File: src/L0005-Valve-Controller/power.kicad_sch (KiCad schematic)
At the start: 29 parts, among them P16 647676-2, P2 140-504-415-000, P9 647676-2, U2 LMS8117AMP-3.3_NOPB, U5 Optocoupler

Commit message: plotted schematic to pdf
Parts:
- C10: value (none) -> 0.1uF
- C11, C14: value (none) -> 2.2uF
- C12, C13: value (none) -> 2.2uF; footprint (none) -> L0005-Valve-Controller:CAP_0603
- C3, C6, C7: value (none) -> 0.1uF; footprint (none) -> L0005-Valve-Controller:CAP_0603
- C8: value (none) -> 4.7uF
- C9: value (none) -> 1uF
- U2: value LMS8117AMP-3.3_NOPB -> (none); footprint L0005-Valve-Controller:LMS8117AMP-3.3NOPB -> (none)
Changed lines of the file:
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@@
       (effects (font (size 1.27 1.27)) (justify left))
     )
-    (property "Value" "" (id 1) (at 154.305 66.04 90)
+    (property "Value" "0.1uF" (id 1) (at 154.305 66.04 90)
       (effects (font (size 1.27 1.27)) (justify left))
     )
@@
       (effects (font (size 1.27 1.27)) (justify left))
     )
-    (property "Value" "" (id 1) (at 166.37 66.04 90)
-      (effects (font (size 1.27 1.27)) (justify left))
-    )
-    (property "Footprint" "" (id 2) (at 163.83 62.23 0)
+    (property "Value" "0.1uF" (id 1) (at 166.37 66.04 90)
+      (effects (font (size 1.27 1.27)) (justify left))
+    )
+    (property "Footprint" "L0005-Valve-Controller:CAP_0603" (id 2) (at 163.83 62.23 0)
       (effects (font (size 1.27 1.27)) (justify left bottom) hide)
     )
@@
       (effects (font (size 1.27 1.27)) (justify left))
     )
-    (property "Value" "" (id 1) (at 245.745 59.69 90)
+    (property "Value" "2.2uF" (id 1) (at 245.745 59.69 90)
       (effects (font (size 1.27 1.27)) (justify left))
     )
@@
       (effects (font (size 1.27 1.27)) (justify left))
     )
-    (property "Value" "" (id 1) (at 203.835 59.69 90)
+    (property "Value" "2.2uF" (id 1) (at 203.835 59.69 90)
       (effects (font (size 1.27 1.27)) (justify left))
     )
@@
       (effects (font (size 1.27 1.27)) (justify left))
     )
-    (property "Value" "" (id 1) (at 215.9 59.69 90)
-      (effects (font (size 1.27 1.27)) (justify left))
-    )
-    (property "Footprint" "" (id 2) (at 213.36 55.88 0)
+    (property "Value" "2.2uF" (id 1) (at 215.9 59.69 90)
+      (effects (font (size 1.27 1.27)) (justify left))
+    )
+    (property "Footprint" "L0005-Valve-Controller:CAP_0603" (id 2) (at 213.36 55.88 0)
       (effects (font (size 1.27 1.27)) (justify left bottom) hide)
     )
@@
       (effects (font (size 1.27 1.27)) (justify left))
     )
-    (property "Value" "" (id 1) (at 234.315 59.69 90)
-      (effects (font (size 1.27 1.27)) (justify left))
-    )
-    (property "Footprint" "" (id 2) (at 231.775 55.88 0)
+    (property "Value" "2.2uF" (id 1) (at 234.315 59.69 90)
+      (effects (font (size 1.27 1.27)) (justify left))
+    )
+    (property "Footprint" "L0005-Valve-Controller:CAP_0603" (id 2) (at 231.775 55.88 0)
       (effects (font (size 1.27 1.27)) (justify left bottom) hide)
     )
@@
       (effects (font (size 1.27 1.27)) (justify left))
     )
-    (property "Value" "" (id 1) (at 127 66.04 90)
+    (property "Value" "4.7uF" (id 1) (at 127 66.04 90)
       (effects (font (size 1.27 1.27)) (justify left))
     )
@@
       (effects (font (size 1.27 1.27)) (justify left))
     )
-    (property "Value" "" (id 1) (at 127.635 51.435 90)
-      (effects (font (size 1.27 1.27)) (justify left))
-    )
-    (property "Footprint" "" (id 2) (at 125.095 47.625 0)
+    (property "Value" "0.1uF" (id 1) (at 127.635 51.435 90)
+      (effects (font (size 1.27 1.27)) (justify left))
+    )
+    (property "Footprint" "L0005-Valve-Controller:CAP_0603" (id 2) (at 125.095 47.625 0)
       (effects (font (size 1.27 1.27)) (justify left bottom) hide)
     )
@@
       (effects (font (size 1.27 1.27)) (justify left))
     )
-    (property "Value" "" (id 1) (at 140.97 66.04 90)
+    (property "Value" "1uF" (id 1) (at 140.97 66.04 90)
       (effects (font (size 1.27 1.27)) (justify left))
     )
@@
       (effects (font (size 1.27 1.27)) (justify left))
     )
-    (property "Value" "" (id 1) (at 165.735 51.435 90)
-      (effects (font (size 1.27 1.27)) (justify left))
-    )
-    (property "Footprint" "" (id 2) (at 163.195 47.625 0)
+    (property "Value" "0.1uF" (id 1) (at 165.735 51.435 90)
+      (effects (font (size 1.27 1.27)) (justify left))
+    )
+    (property "Footprint" "L0005-Valve-Controller:CAP_0603" (id 2) (at 163.195 47.625 0)
       (effects (font (size 1.27 1.27)) (justify left bottom) hide)
     )
@@
     (in_bom yes) (on_board yes)
     (property "Reference" "U2" (id 0) (at 55.88 48.3108 0))
-    (property "Value" "LMS8117AMP-3.3_NOPB" (id 1) (at 55.88 48.2854 0)
-      (effects (font (size 1.27 1.27)) hide)
-    )
-    (property "Footprint" "L0005-Valve-Controller:LMS8117AMP-3.3NOPB" (id 2) (at 55.88 53.975 0)
-      (effects (font (size 1.27 1.27)) hide)
-    )
+    (property "Value" "" (id 1) (at 55.88 48.2854 0)
+      (effects (font (size 1.27 1.27)) hide)
+    )
+    (property "Footprint" "" (id 2) (at 55.88 53.975 0)
+      (effects (font (size 1.27 1.27)) hide)
+    )

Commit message: routed rev 2
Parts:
- C10, C11, C14, C8, C9: footprint (none) -> L0005-Valve-Controller:CAP_0603
- U2: value (none) -> LMS8117AMP-3.3_NOPB; footprint (none) -> L0005-Valve-Controller:LMS8117AMP-3.3NOPB
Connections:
- net Earth: now also C11.1, C12.1, C13.1, C14.1
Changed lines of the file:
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@@
   (junction (at 223.52 63.5) (diameter 0) (color 0 0 0 0)
   )
+  (junction (at 232.41 63.5) (diameter 0) (color 0 0 0 0)
+  )
   (junction (at 151.13 45.085) (diameter 0) (color 0 0 0 0)
   )
@@
     (stroke (width 0) (type default) (color 0 0 0 0))
   )
-  (wire (pts (xy 223.52 63.5) (xy 241.935 63.5))
+  (wire (pts (xy 223.52 63.5) (xy 232.41 63.5))
     (stroke (width 0) (type default) (color 0 0 0 0))
   )
@@
     (stroke (width 0) (type default) (color 0 0 0 0))
   )
+  (wire (pts (xy 232.41 63.5) (xy 241.935 63.5))
+    (stroke (width 0) (type default) (color 0 0 0 0))
+  )
   (wire (pts (xy 235.585 53.34) (xy 241.935 53.34))
     (stroke (width 0) (type default) (color 0 0 0 0))
@@
   )
   (polyline (pts (xy 22.225 141.605) (xy 22.225 93.345))
+    (stroke (width 0) (type default) (color 0 0 0 0))
+  )
+  (wire (pts (xy 232.41 63.5) (xy 232.41 65.405))
     (stroke (width 0) (type default) (color 0 0 0 0))
   )
@@
       (effects (font (size 1.27 1.27)) (justify left))
     )
-    (property "Footprint" "" (id 2) (at 151.765 62.23 0)
+    (property "Footprint" "L0005-Valve-Controller:CAP_0603" (id 2) (at 151.765 62.23 0)
       (effects (font (size 1.27 1.27)) (justify left bottom) hide)
     )
@@
       (effects (font (size 1.27 1.27)) (justify left))
     )
-    (property "Footprint" "" (id 2) (at 243.205 55.88 0)
+    (property "Footprint" "L0005-Valve-Controller:CAP_0603" (id 2) (at 243.205 55.88 0)
       (effects (font (size 1.27 1.27)) (justify left bottom) hide)
     )
@@
       (effects (font (size 1.27 1.27)) (justify left))
     )
-    (property "Footprint" "" (id 2) (at 201.295 55.88 0)
+    (property "Footprint" "L0005-Valve-Controller:CAP_0603" (id 2) (at 201.295 55.88 0)
       (effects (font (size 1.27 1.27)) (justify left bottom) hide)
     )
@@
       (effects (font (size 1.27 1.27)) (justify left))
     )
-    (property "Footprint" "" (id 2) (at 125.095 62.23 0)
+    (property "Footprint" "L0005-Valve-Controller:CAP_0603" (id 2) (at 125.095 62.23 0)
       (effects (font (size 1.27 1.27)) (justify left bottom) hide)
     )
@@
       (effects (font (size 1.27 1.27)) (justify left))
     )
-    (property "Footprint" "" (id 2) (at 137.16 62.23 0)
+    (property "Footprint" "L0005-Valve-Controller:CAP_0603" (id 2) (at 137.16 62.23 0)
       (effects (font (size 1.27 1.27)) (justify left bottom) hide)
     )
@@
     (pin "1")
     (pin "2")
+  )
+  (symbol (lib_id "L0005-Valve-Controller:Earth") (at 232.41 65.405 0) (unit 1)
+    (in_bom yes) (on_board yes)
+    (property "Reference" "#PWR?" (id 0) (at 232.41 71.755 0)
+      (effects (font (size 1.27 1.27)) hide)
+    )
+    (property "Value" "Earth" (id 1) (at 232.41 69.215 0)
+      (effects (font (size 1.27 1.27)) hide)
+    )
+    (property "Footprint" "" (id 2) (at 232.41 65.405 0)
+      (effects (font (size 1.27 1.27)) hide)
+    )
+    (property "Datasheet" "" (id 3) (at 232.41 65.405 0)
+      (effects (font (size 1.27 1.27)) hide)
+    )
+    (pin "1")
   )
   (symbol (lib_id "L0005-Valve-Controller:LED_GREEN") (at 86.995 60.325 0) (unit 1)
@@
     (in_bom yes) (on_board yes)
     (property "Reference" "U2" (id 0) (at 55.88 48.3108 0))
-    (property "Value" "" (id 1) (at 55.88 48.2854 0)
-      (effects (font (size 1.27 1.27)) hide)
-    )
-    (property "Footprint" "" (id 2) (at 55.88 53.975 0)
-      (effects (font (size 1.27 1.27)) hide)
-    )
+    (property "Value" "LMS8117AMP-3.3_NOPB" (id 1) (at 55.88 48.2854 0)
+      (effects (font (size 1.27 1.27)) hide)
+    )
+    (property "Footprint" "L0005-Valve-Controller:LMS8117AMP-3.3NOPB" (id 2) (at 55.88 53.975 0)
+      (effects (font (size 1.27 1.27)) hide)
+    )

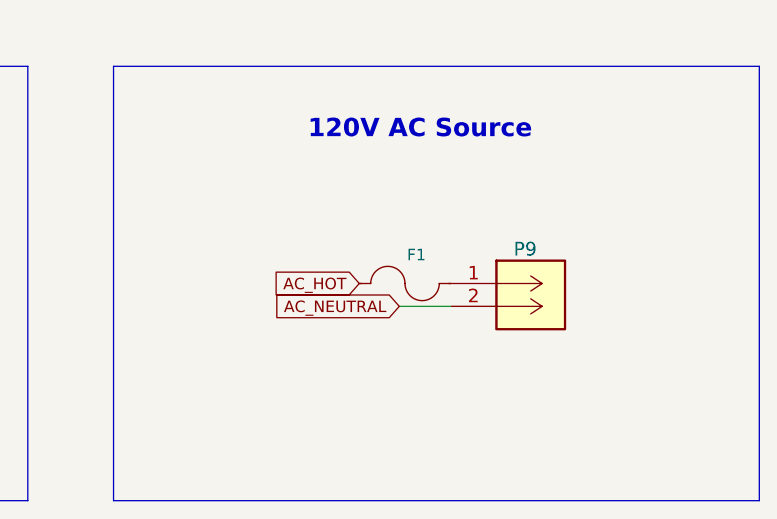
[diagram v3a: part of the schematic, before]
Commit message: added NO jumper to MCU reset button
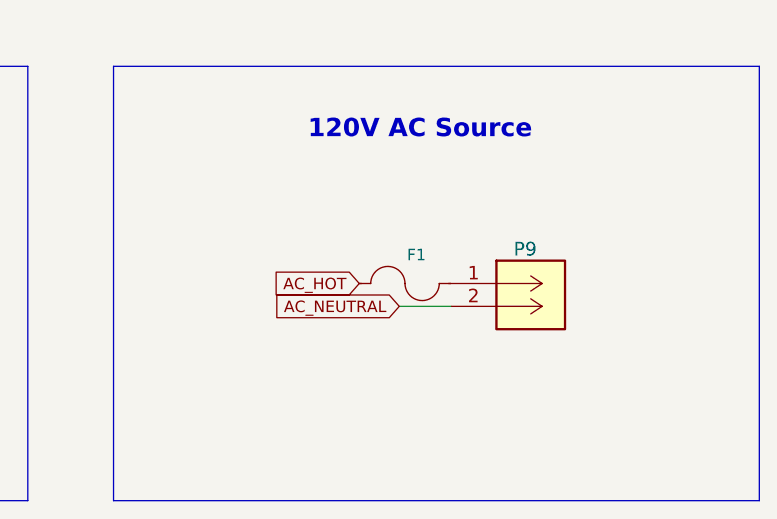
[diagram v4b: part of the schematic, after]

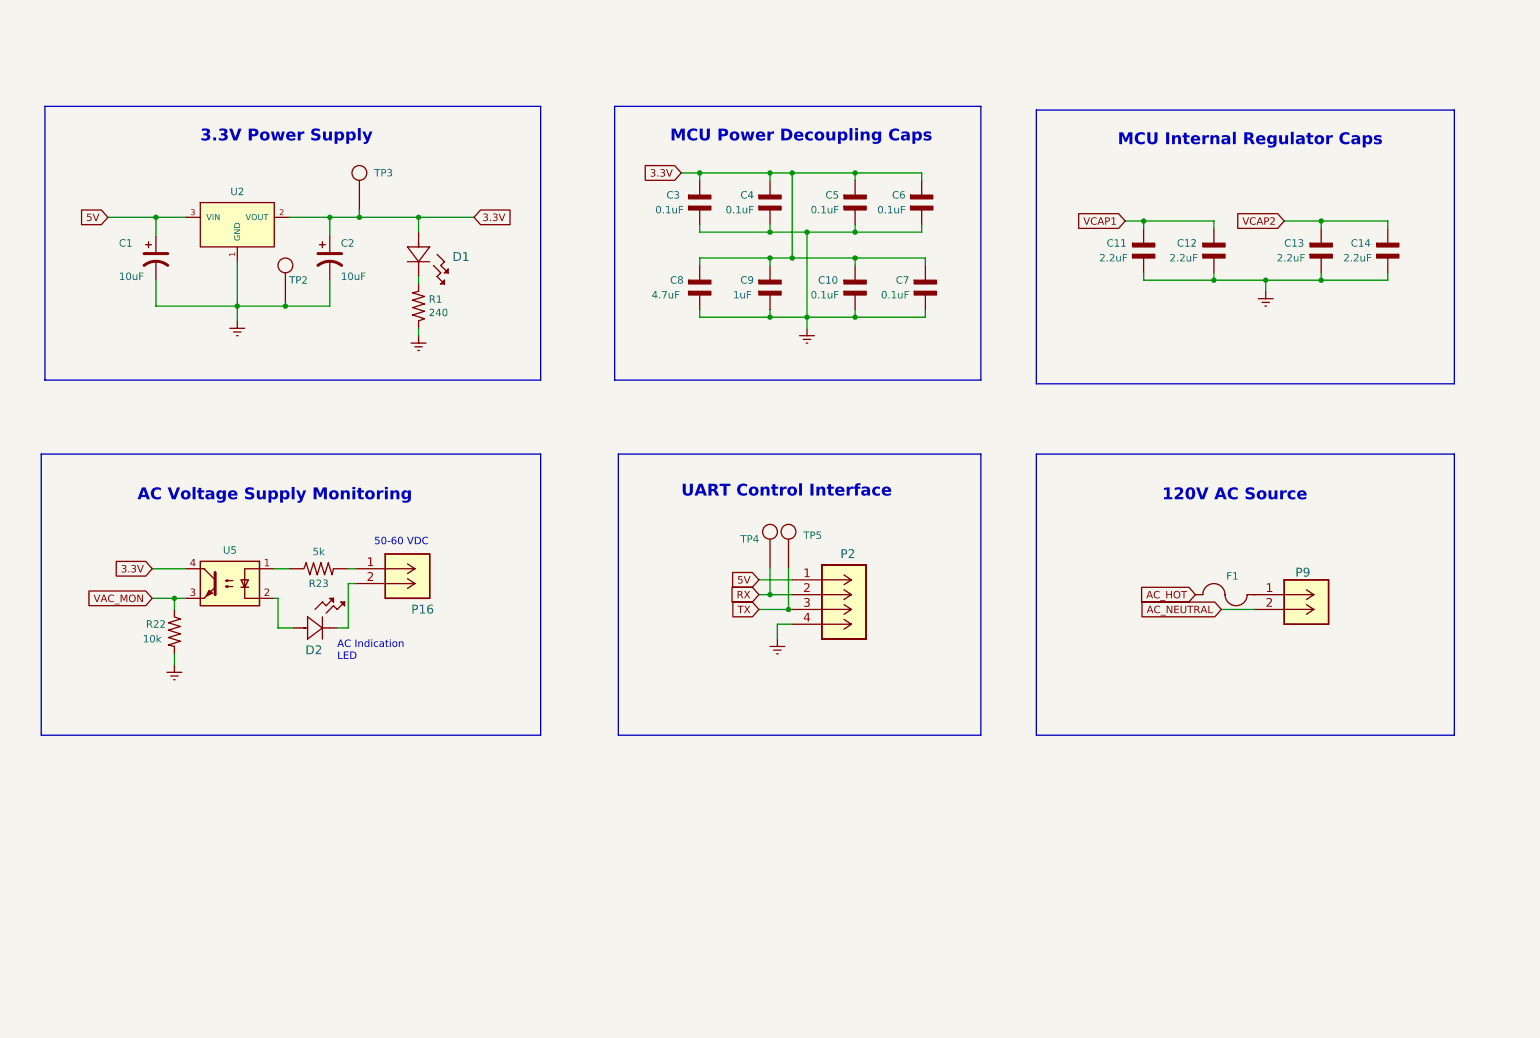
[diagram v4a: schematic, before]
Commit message: added USB to lib files and schematic
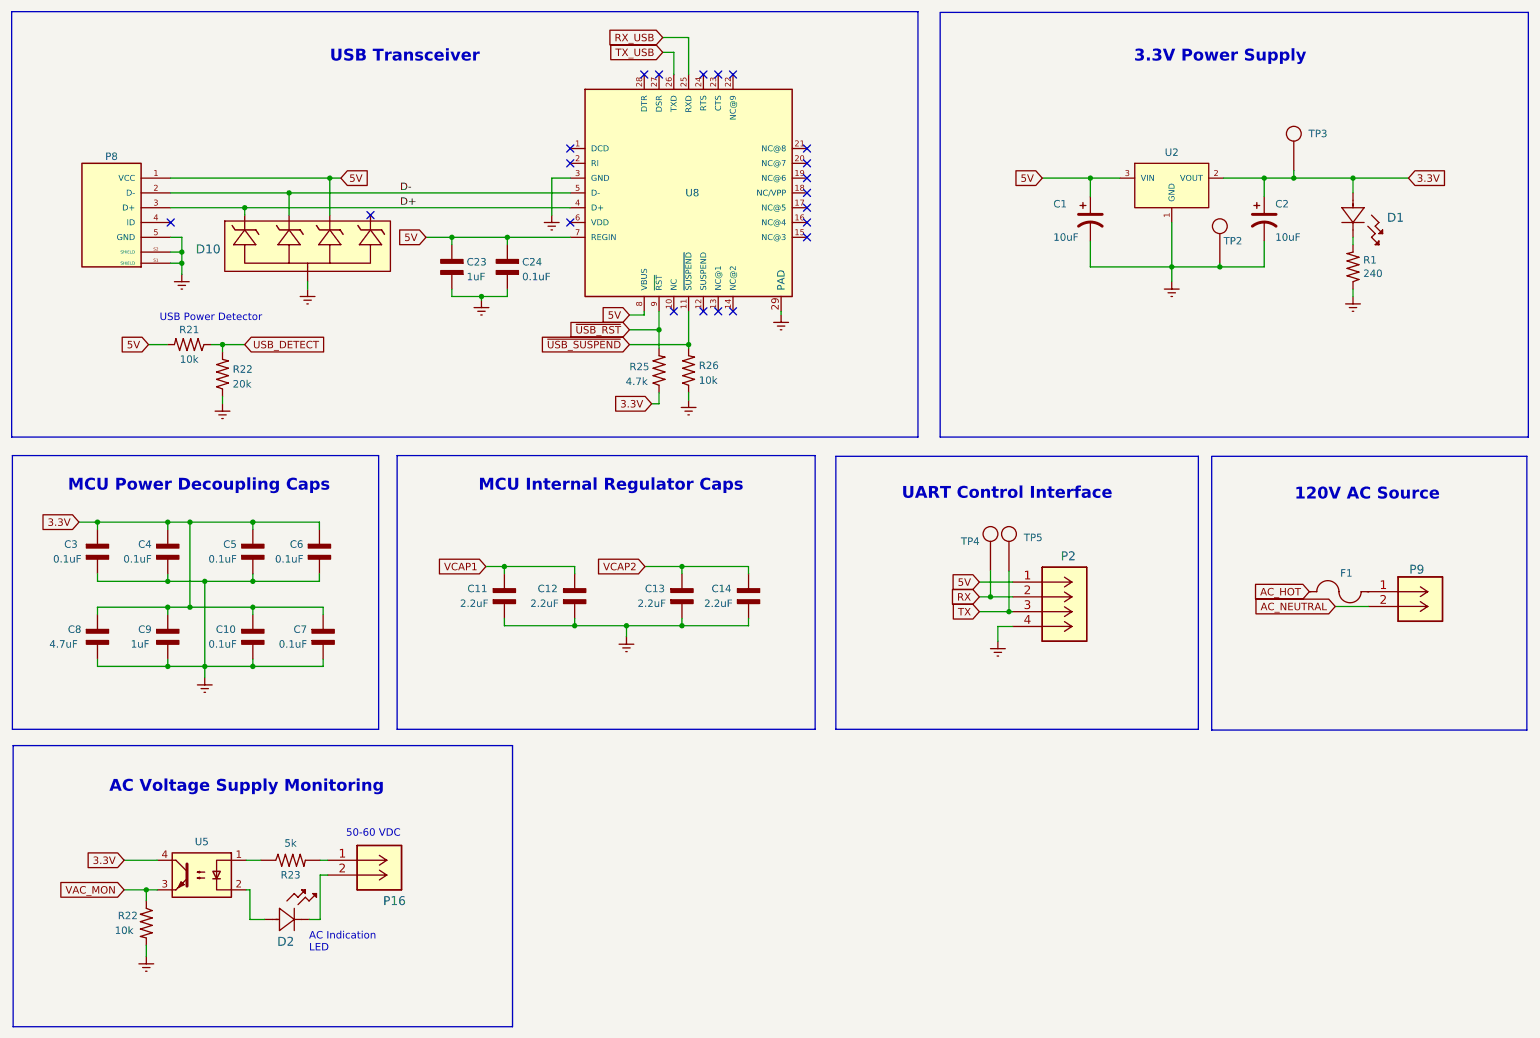
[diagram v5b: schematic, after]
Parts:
- added C23: 1uF, Flight-Computer:CAP_0603, symbol Flight-Computer:CAP_0603
- added C24: 0.1uF, Flight-Computer:CAP_0603, symbol Flight-Computer:CAP_0603
- added D10: SP0504BAHTG, SOD-123FL_MCC, symbol Flight-Computer:SP0504BAHTG
- added P8: USB, BEL_SS-52300-001, symbol Flight-Computer:USB
- added R21, R26: 10k, Flight-Computer:RES_0603, symbol Flight-Computer:RES_0603
- added R22: 20k, Flight-Computer:RES_0603, symbol Flight-Computer:RES_0603
- added R25: 4.7k, Flight-Computer:RES_0603, symbol Flight-Computer:RES_0603
- added U8: CP2102-GMR(QFN28), QFN28G_0.5-5X5MM, symbol Flight-Computer:CP2102-GMR(QFN28)
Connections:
- net 3.3V: now also R25.1
- net 5V: now also C23.1, C24.1, D10.4, P8.1 (VCC), R21.2, U8.7 (REGIN), U8.8 (VBUS)
- net Earth: now also C23.2, C24.2, D10.2, P8.5 (GND), P8.S1 (SHIELD), P8.S2 (SHIELD), R22.1, R26.1, U8.29 (PAD), U8.3 (GND)
- new net D+: D10.1, P8.3 (D+), U8.4 (D+)
- new net D-: D10.3, P8.2 (D-), U8.5 (D-)
- new net RX_USB: U8.25 (RXD)
- new net TX_USB: U8.26 (TXD)
- new net USB_DETECT: R21.1, R22.2
- new net ~{USB_RST}: R25.2, U8.9 (~{RST})
- new net ~{USB_SUSPEND}: R26.2, U8.11 (~{SUSPEND})
- no-connect marks 0 -> 21
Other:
- note added: "USB Power Detector"
- note added: "USB Transceiver"
- moved on the sheet: C1, C10, C11, C12, C13, C14, C2, C3, C4, C5, C6, C7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

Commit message: finalized schematic
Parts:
- C23, C24: footprint Flight-Computer:CAP_0603 -> L0005-Valve-Controller:CAP_0603
- D10: footprint SOD-123FL_MCC -> L0005-Valve-Controller:SP0504BAHTG
- P8: footprint BEL_SS-52300-001 -> L0005-Valve-Controller:USB-TypeB
- R21, R22, R25, R26: footprint Flight-Computer:RES_0603 -> L0005-Valve-Controller:RES_0603
- U8: footprint QFN28G_0.5-5X5MM -> L0005-Valve-Controller:RES_0603
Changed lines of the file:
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@@
       (effects (font (size 1.27 1.27)) (justify left bottom) hide)
     )
-    (property "Footprint" "QFN28G_0.5-5X5MM" (at 97.79 75.184 0)
+    (property "Footprint" "L0005-Valve-Controller:RES_0603" (at 97.79 75.184 0)
       (effects (font (size 1.27 1.27)) (justify left bottom) hide)
     )
@@
       (effects (font (size 1.27 1.27)) (justify right))
     )
-    (property "Footprint" "Flight-Computer:RES_0603" (at 146.05 77.724 0)
+    (property "Footprint" "L0005-Valve-Controller:RES_0603" (at 146.05 77.724 0)
       (effects (font (size 1.27 1.27)) (justify left bottom) hide)
     )
@@
       (effects (font (size 1.27 1.27)))
     )
-    (property "Footprint" "Flight-Computer:RES_0603" (at 46.355 61.849 0)
+    (property "Footprint" "L0005-Valve-Controller:RES_0603" (at 46.355 61.849 0)
       (effects (font (size 1.27 1.27)) (justify left bottom) hide)
     )
@@
       (effects (font (size 1.27 1.27)) (justify right))
     )
-    (property "Footprint" "Flight-Computer:CAP_0603" (at 112.395 63.754 0)
+    (property "Footprint" "L0005-Valve-Controller:CAP_0603" (at 112.395 63.754 0)
       (effects (font (size 1.27 1.27)) (justify left bottom) hide)
     )
@@
       (effects (font (size 1.27 1.27)) (justify right))
     )
-    (property "Footprint" "Flight-Computer:RES_0603" (at 66.04 78.359 0)
+    (property "Footprint" "L0005-Valve-Controller:RES_0603" (at 66.04 78.359 0)
       (effects (font (size 1.27 1.27)) (justify left bottom) hide)
     )
@@
       (effects (font (size 1.27 1.27)) (justify right))
     )
-    (property "Footprint" "Flight-Computer:CAP_0603" (at 102.87 63.754 0)
+    (property "Footprint" "L0005-Valve-Controller:CAP_0603" (at 102.87 63.754 0)
       (effects (font (size 1.27 1.27)) (justify left bottom) hide)
     )
@@
       (effects (font (size 1.27 1.27)) (justify right))
     )
-    (property "Footprint" "Flight-Computer:RES_0603" (at 140.97 77.724 0)
+    (property "Footprint" "L0005-Valve-Controller:RES_0603" (at 140.97 77.724 0)
       (effects (font (size 1.27 1.27)) (justify left bottom) hide)
     )
@@
       (effects (font (size 1.27 1.27)) (justify left bottom) hide)
     )
-    (property "Footprint" "BEL_SS-52300-001" (at 43.18 68.834 0)
+    (property "Footprint" "L0005-Valve-Controller:USB-TypeB" (at 43.18 68.834 0)
       (effects (font (size 1.27 1.27)) (justify left bottom) hide)
     )
@@
       (effects (font (size 1.524 1.524)) hide)
     )
-    (property "Footprint" "SOD-123FL_MCC" (at 47.117 78.359 0)
+    (property "Footprint" "L0005-Valve-Controller:SP0504BAHTG" (at 47.117 78.359 0)
       (effects (font (size 1.524 1.524)) hide)
     )

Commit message: routed rev3
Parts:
- removed P8: USB, L0005-Valve-Controller:USB-TypeB, symbol Flight-Computer:USB
- added P17: USB, L0005-Valve-Controller:USB-TypeB, symbol L0005-Valve-Controller:USB
- U8: footprint L0005-Valve-Controller:RES_0603 -> L0005-Valve-Controller:CP2012-GMR
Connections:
- net 5V: now also D10.5, P17.1 (VCC); no longer D10.4
- net D+: now also D10.3, P17.3 (D+); no longer D10.1
- net D-: now also D10.1, P17.2 (D-); no longer D10.3
- net Earth: now also P17.4 (GND), P17.S1 (SHIELD), P17.S2 (SHIELD)
- no-connect marks 21 -> 20
